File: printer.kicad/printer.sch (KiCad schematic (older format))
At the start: 12 parts

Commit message: Reimplement ZX Spectrum bus interface
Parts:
- removed U? (x4): D3413A, symbol 74xx_IEEE:7413
- removed U? (x5): D3404A, symbol 74xx_IEEE:7404
- added U? (x2): 74AC373, symbol 74xx:74LS373
- added U? (x8): 74HCT02, symbol 74xx:74HCT02
- added U? (x4): 74HCT00, symbol 74xx:74HCT00
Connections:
- net labels added: DEVICE_RD, DEVICE_WR, ENCODER, MOTOR_SLOW, MOTOR_STOP, PAPER, READY, STYLUS, ~ENCODER_LATCH, ~PAPER_LATCH, ~STYLUS
- net labels removed: READ|WRITE, WR
- wire segments 58 -> 83
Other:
- note added: "Decoding"
- note added: "INPUT"
- note added: "Latches"
- note added: "OUTPUT"
- moved on the sheet: J?, U?

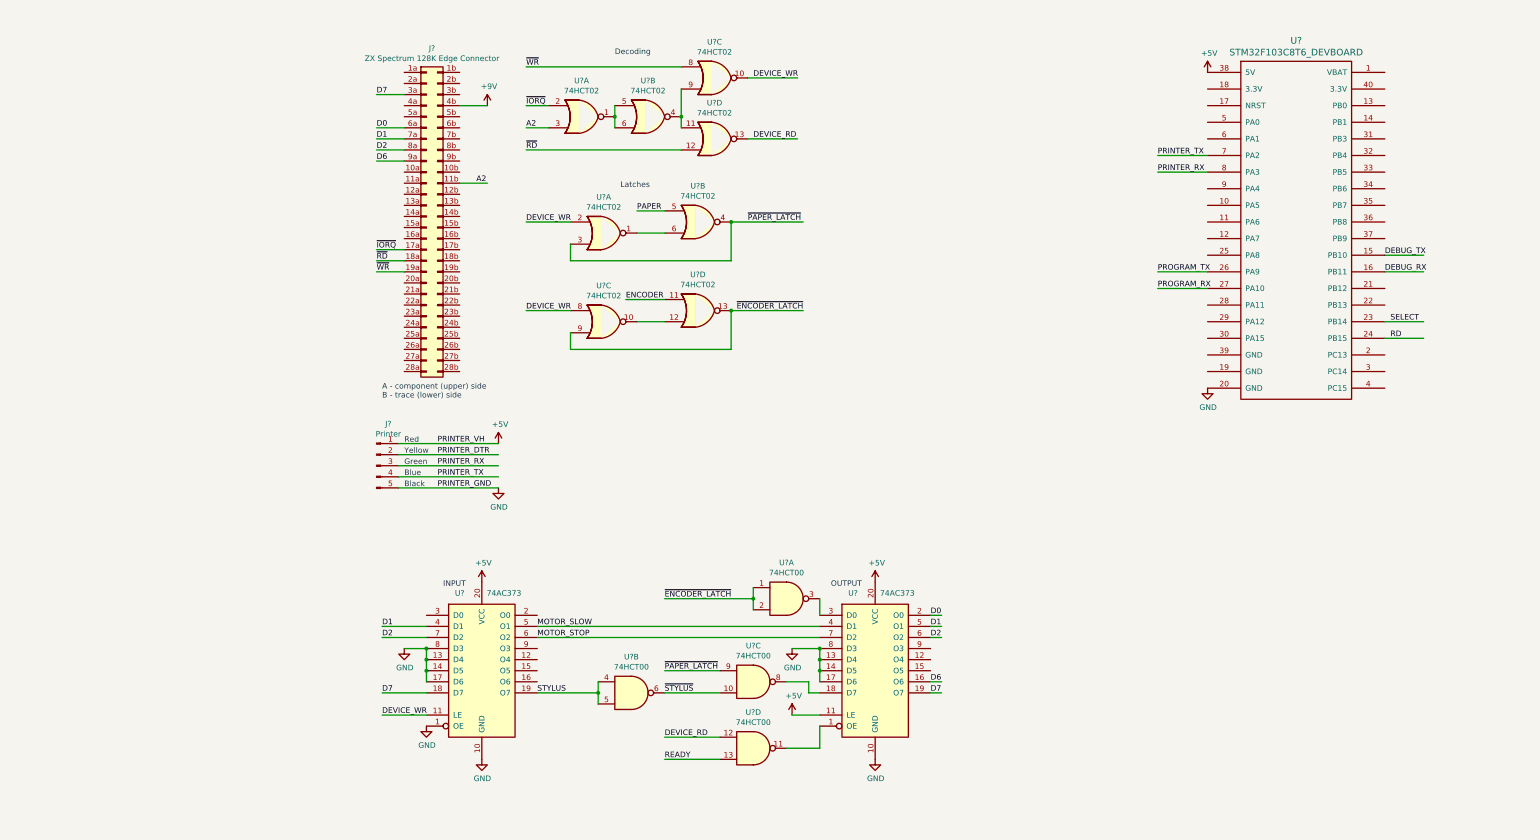
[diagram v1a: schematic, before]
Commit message: Redo latching in HW, understand interface better
Redo latching in hardware, only to understand after testing that the
interface is different. The printer is supposed to reset the latches on
every write regardless of the encoder and paper position.
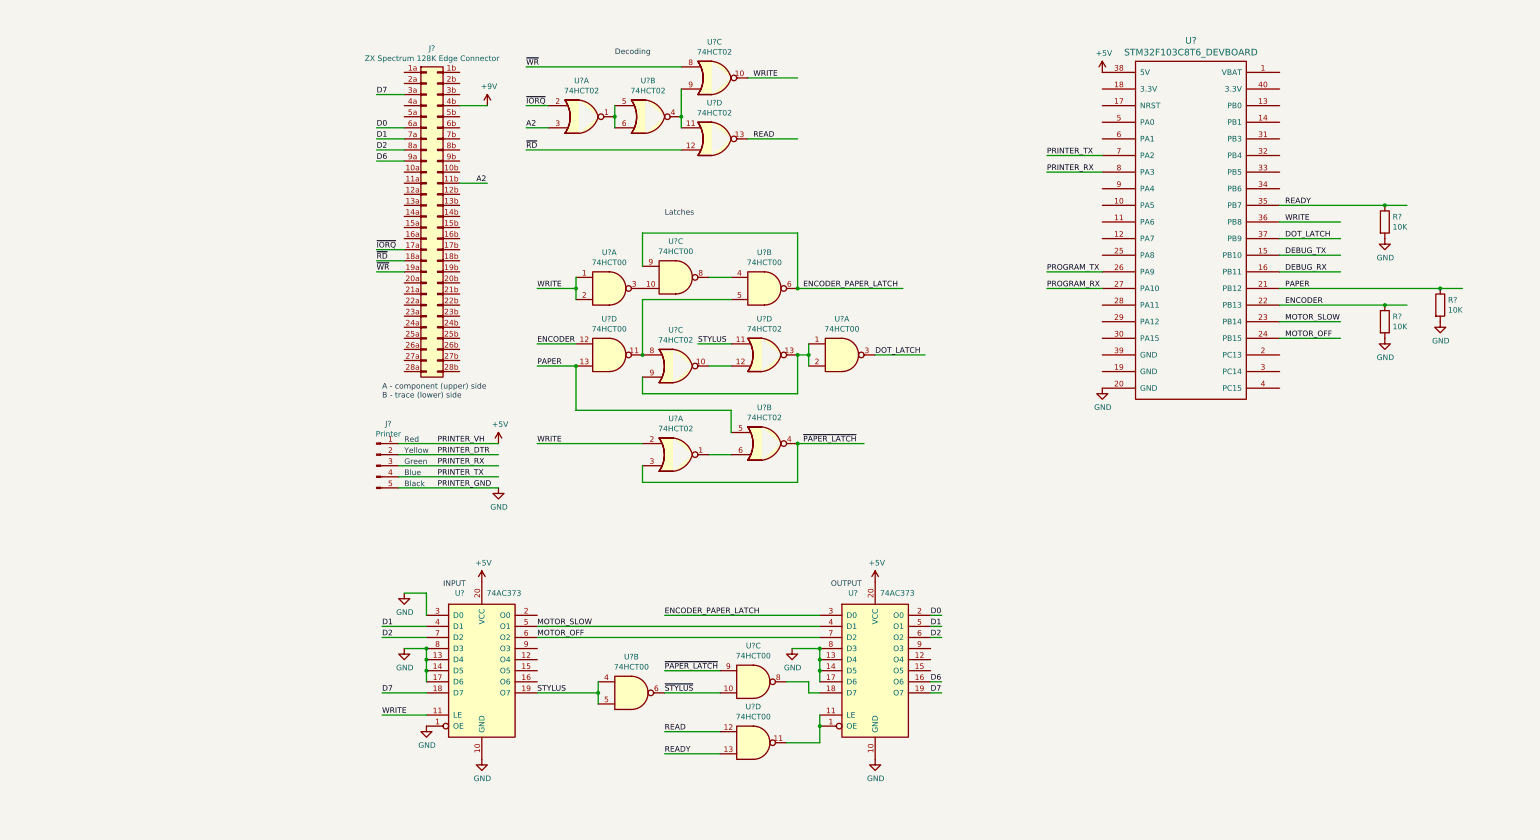
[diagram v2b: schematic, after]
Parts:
- removed U? (x3): 74HCT02, symbol 74xx:74HCT02
- removed U? (x2): 74HCT00, symbol 74xx:74HCT00
- added R? (x3): 10K, symbol Device:R
- added U? (x6): 74HCT00, symbol 74xx:74HCT00
- added U? (x3): 74HCT02, symbol 74xx:74HCT02
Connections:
- net labels added: DOT_LATCH, ENCODER_PAPER_LATCH, MOTOR_OFF, READ, WRITE
- net labels removed: DEVICE_RD, DEVICE_WR, MOTOR_STOP, RD, SELECT, ~ENCODER_LATCH
- wire segments 83 -> 106
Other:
- moved on the sheet: U?, U?A, U?B, U?D

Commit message: Make ZX Printer communication work
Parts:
- removed U? (x5): 74HCT00, symbol 74xx:74HCT00
- removed U? (x4): 74HCT02, symbol 74xx:74HCT02
- added U?: 74HCT00, symbol 74xx:74HCT00
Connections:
- net labels added: ~PAPER
- net labels removed: DOT_LATCH, ENCODER_PAPER_LATCH, ~PAPER_LATCH
- wire segments 106 -> 80
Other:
- note removed: "Latches"
- moved on the sheet: U?, U?B, U?C, U?D

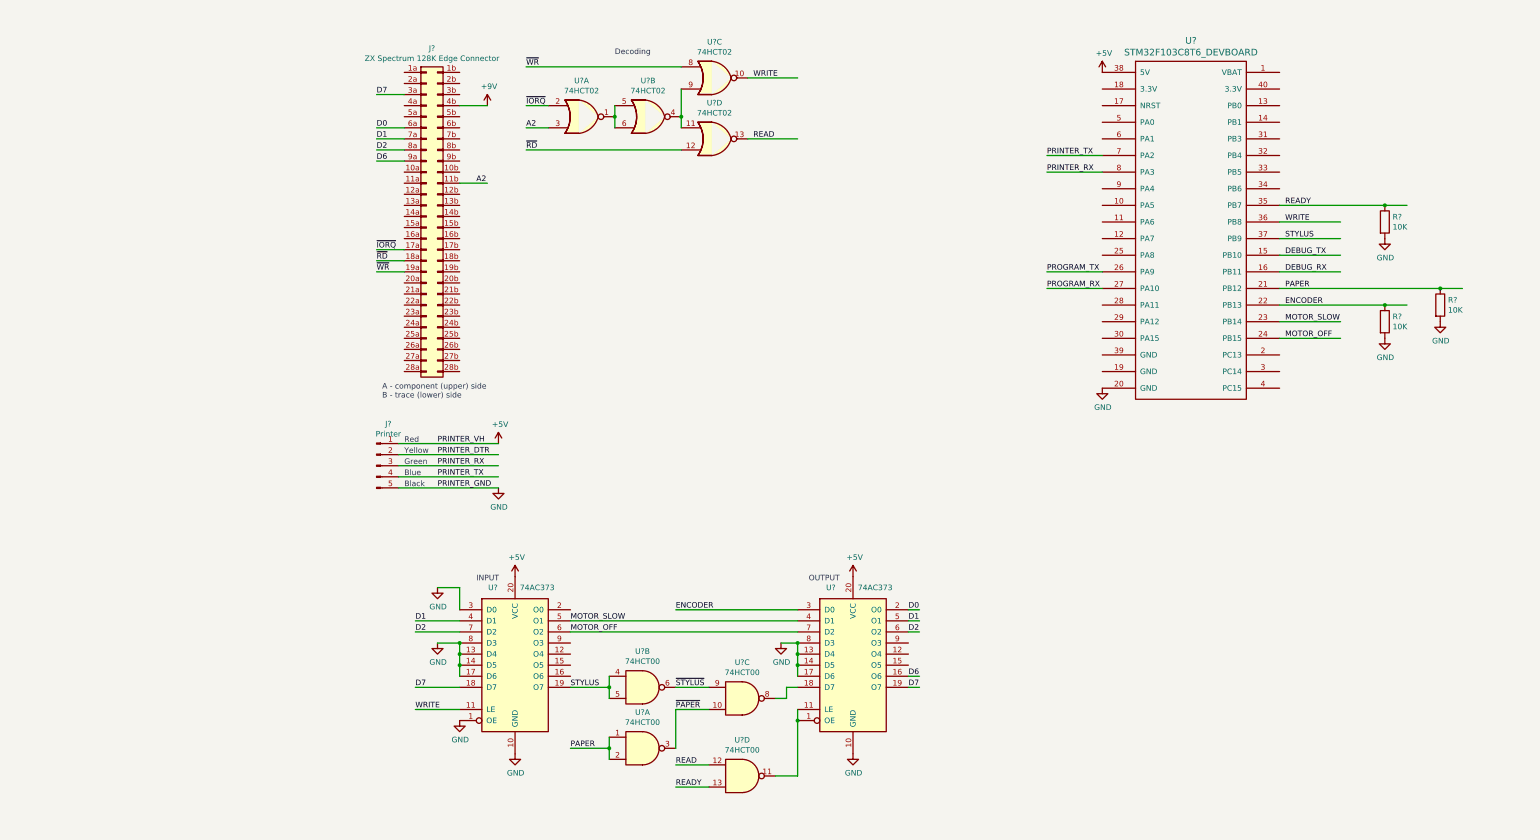
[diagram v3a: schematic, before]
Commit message: Complete schematics for JLCPCB
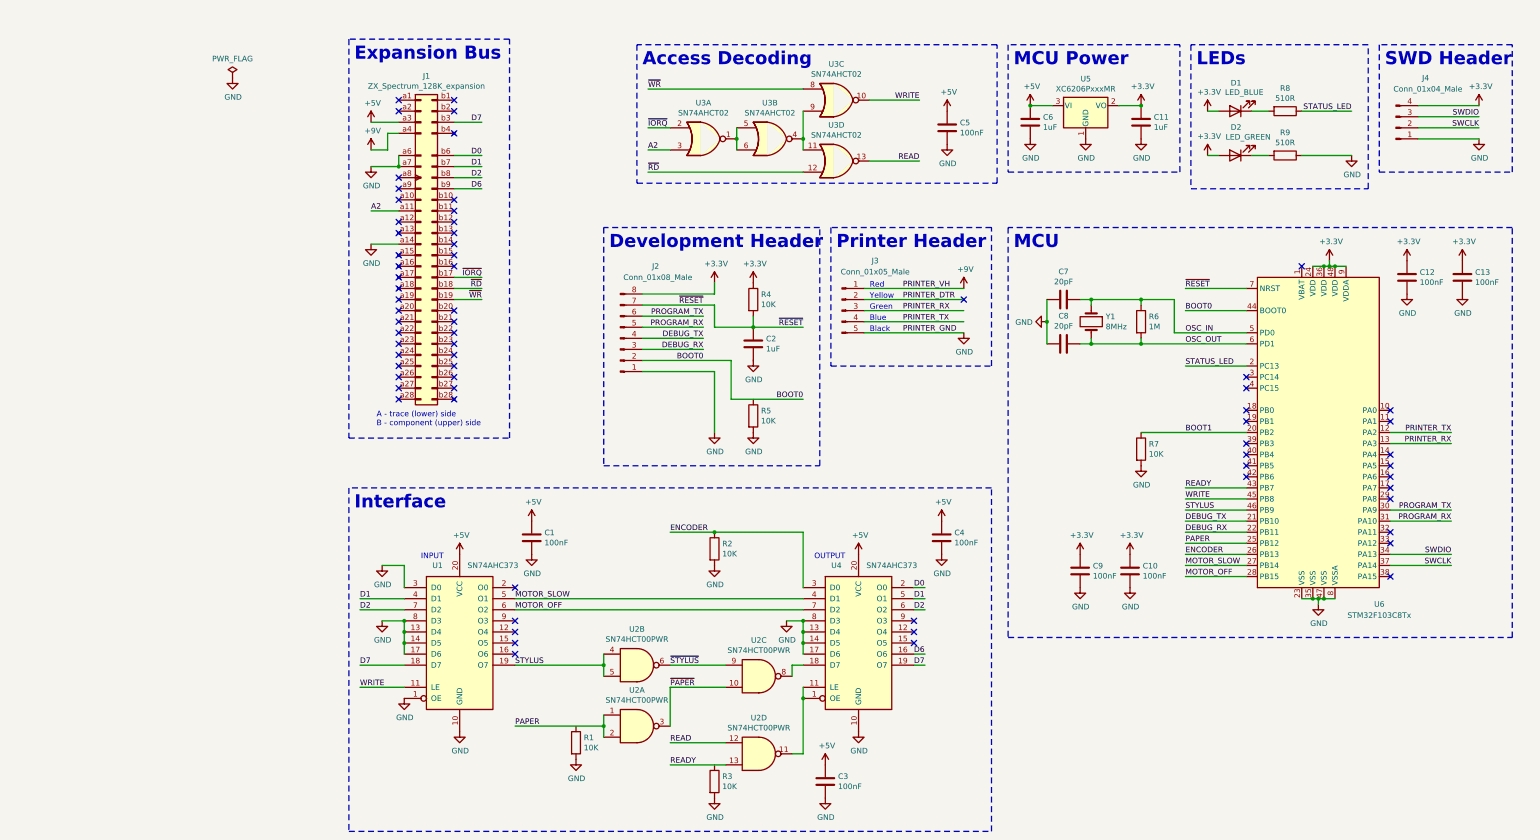
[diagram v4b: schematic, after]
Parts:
- removed J?: ZX Spectrum 128K Edge Connector, symbol Connector_Generic:Conn_02x28_Row_Letter_Last
- removed R? (x2): 10K, symbol Device:R
- removed U?: STM32F103C8T6_DEVBOARD, symbol printer-rescue:STM32F103C8T6_DEVBOARD-printer
- added C1, C10, C12, C13, C3, C4, C5, C9: 100nF, Capacitor_SMD:C_0603_1608Metric, symbol Device:C
- added C11, C2, C6: 1uF, Capacitor_SMD:C_0603_1608Metric, symbol Device:C
- added C7, C8: 20pF, Capacitor_SMD:C_0603_1608Metric, symbol Device:C
- added D1: LED_BLUE, LED_SMD:LED_0603_1608Metric, symbol Device:LED
- added D2: LED_GREEN, LED_SMD:LED_0603_1608Metric, symbol Device:LED
- added J1: ZX_Spectrum_128K_expansion, printer:board_socket, symbol printer:ZX_Spectrum_128K_expansion
- added J2: Conn_01x08_Male, Connector_PinHeader_2.54mm:PinHeader_1x08_P2.54mm_Vertical, symbol Connector:Conn_01x08_Male
- added J4: Conn_01x04_Male, Connector_PinHeader_2.54mm:PinHeader_1x04_P2.54mm_Vertical, symbol Connector:Conn_01x04_Male
- added R1, R3, R4, R5, R7: 10K, Resistor_SMD:R_0603_1608Metric, symbol Device:R
- added R6: 1M, Resistor_SMD:R_0603_1608Metric, symbol Device:R
- added R8, R9: 510R, Resistor_SMD:R_0603_1608Metric, symbol Device:R
- added U5: XC6206PxxxMR, Package_TO_SOT_SMD:SOT-23, symbol Master_Regulator_Linear:XC6206PxxxMR
- added U6: STM32F103C8Tx, Package_QFP:LQFP-48_7x7mm_P0.5mm, symbol MCU_ST_STM32F1:STM32F103C8Tx
- added Y1: 8MHz, Crystal:Crystal_SMD_5032-2Pin_5.0x3.2mm, symbol Device:Crystal
- J3: renamed from J?; value Printer -> Conn_01x05_Male; footprint (none) -> Connector_JST:JST_XH_B5B-XH-A_1x05_P2.50mm_Vertical
- R2: renamed from R?; footprint (none) -> Resistor_SMD:R_0603_1608Metric; LCSC (none) -> C25804
- U1, U4: renamed from U?; value 74AC373 -> SN74AHC373; footprint (none) -> Package_SO:TSSOP-20_4.4x6.5mm_P0.65mm; LCSC (none) -> C80242
- U2: renamed from U?; value 74HCT00 -> SN74HCT00PWR; footprint (none) -> Package_SO:TSSOP-14_4.4x5mm_P0.65mm; LCSC (none) -> C131694
- U3: renamed from U?; value 74HCT02 -> SN74AHCT02; footprint (none) -> Package_SO:TSSOP-14_4.4x5mm_P0.65mm; LCSC (none) -> C87964
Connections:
- net labels added: +3.3V, BOOT0, BOOT1, OSC_IN, OSC_OUT, STATUS_LED, SWCLK, SWDIO, ~IORQ, ~RD, ~RESET, ~WR
- net labels removed: ~IORQ~, ~RD~, ~WR~
- wire segments 80 -> 142
- no-connect marks 0 -> 68
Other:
- note added: "A - trace (lower) side\nB - component (upper) side\n"
- note added: "Access Decoding"
- note added: "Development Header"
- note added: "Expansion Bus"
- note added: "Interface"
- note added: "LEDs"
- note added: "MCU"
- note added: "MCU Power"
- note added: "Printer Header"
- note added: "SWD Header"
- note removed: "A - component (upper) side\nB - trace (lower) side"
- note removed: "Decoding"
- moved on the sheet: J3, R2, U1, U2A, U2B, U2C, U2D, U3A, U3B, U3C, U3D, U4

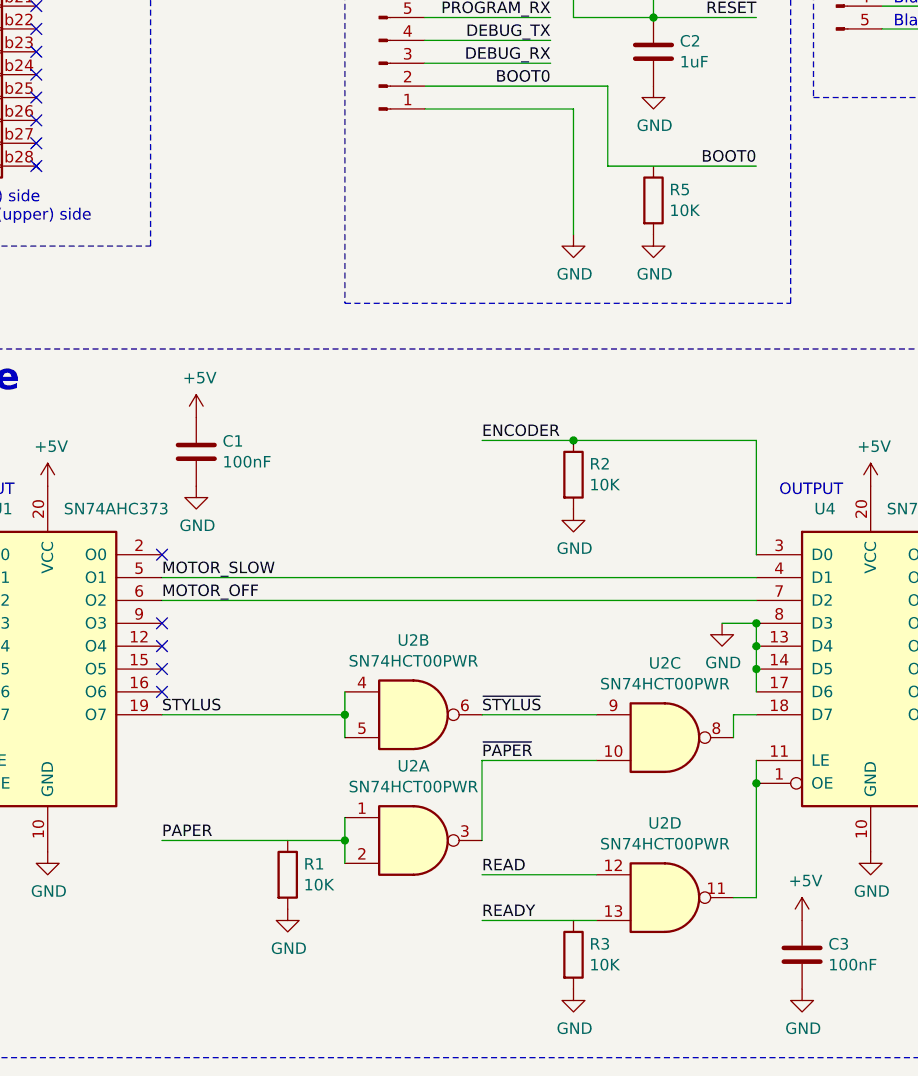
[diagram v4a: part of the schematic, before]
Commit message: Fix unconnected resistors on schematics
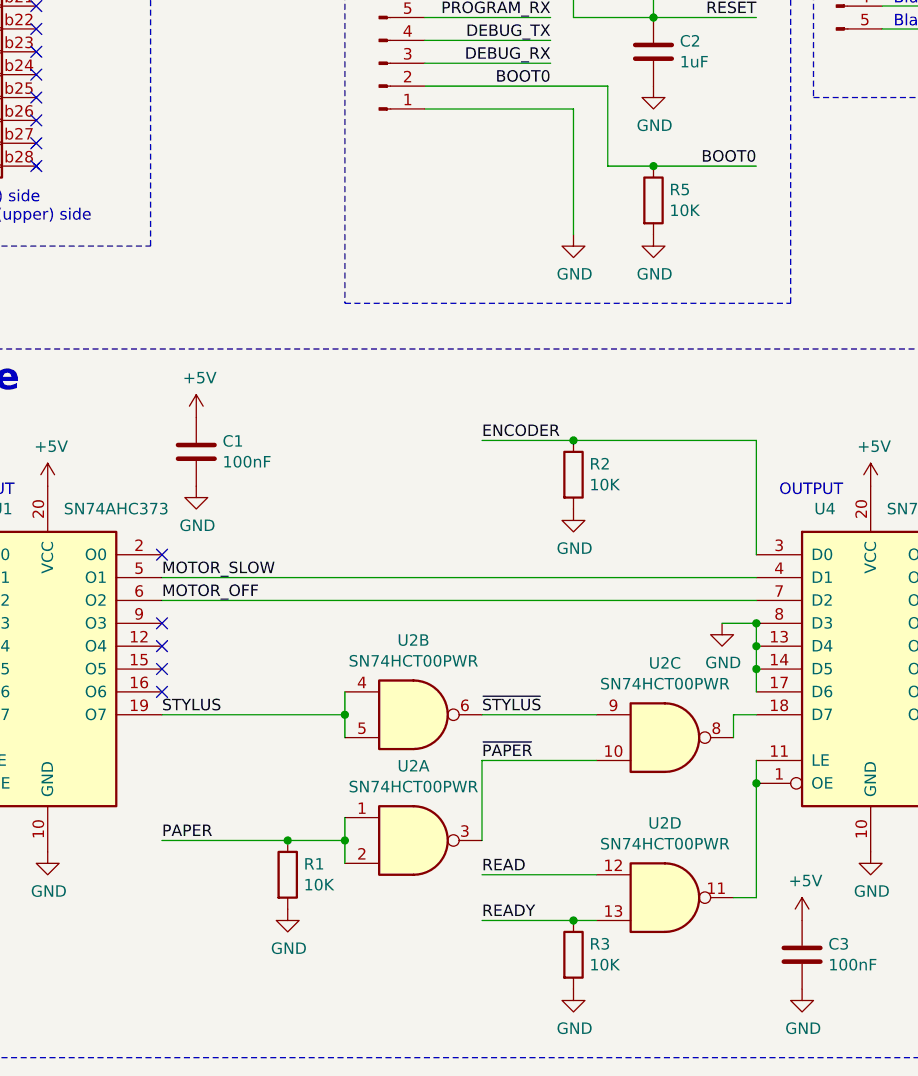
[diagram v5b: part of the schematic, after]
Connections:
- wire segments 142 -> 145
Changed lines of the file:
@@
 NoConn ~ 8700 3600
 Wire Wire Line
-	3500 7100 4000 7100
+	3500 7100 3900 7100
 $Comp
 L Device:R R3
@@
 $EndComp
 Wire Wire Line
-	2100 6750 2900 6750
+	2100 6750 2650 6750
 $Comp
 L Device:R R1
@@
 $EndComp
 Wire Wire Line
-	4050 3800 4700 3800
+	4050 3800 4250 3800
 $Comp
 L Device:R R5
@@
 	-1   0    0    1
 $EndComp
+Connection ~ 3900 7100
+Wire Wire Line
+	3900 7100 4000 7100
+Connection ~ 2650 6750
+Wire Wire Line
+	2650 6750 2900 6750
+Connection ~ 4250 3800
+Wire Wire Line
+	4250 3800 4700 3800
 $EndSCHEMATC

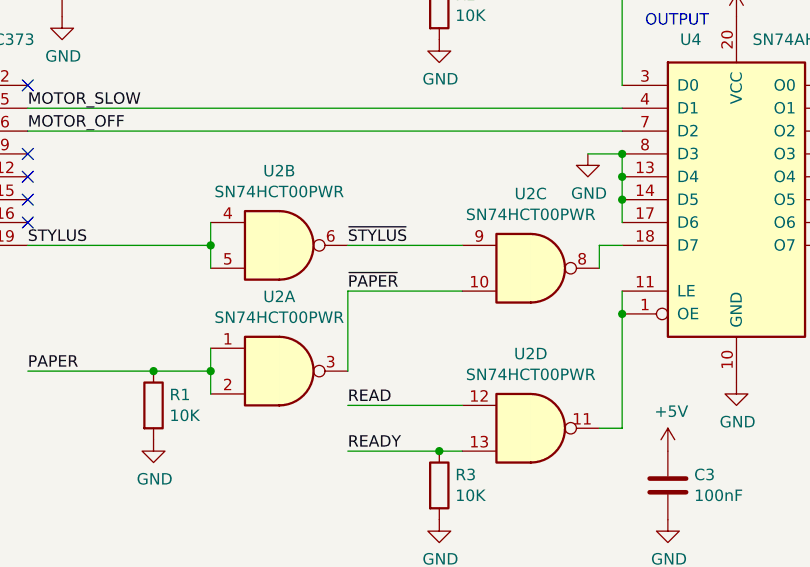
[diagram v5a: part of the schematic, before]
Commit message: Shorten SN74HCT00PWR to SN74HCT00
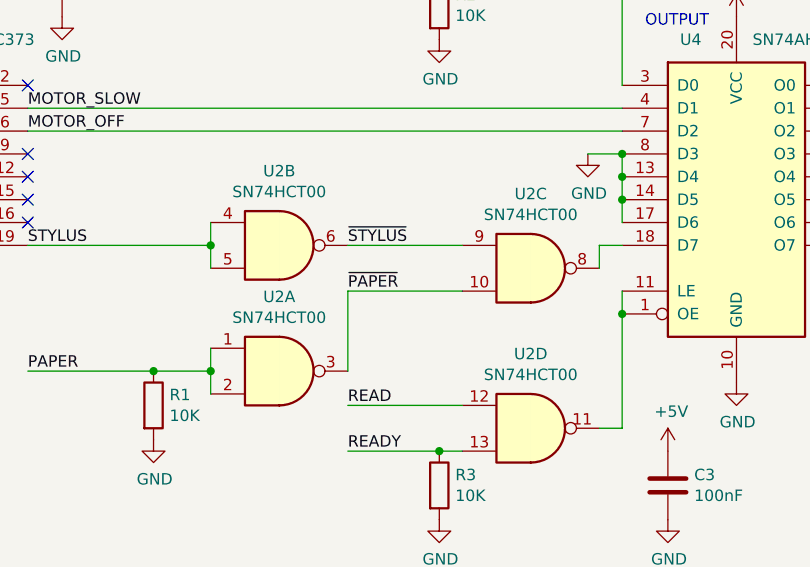
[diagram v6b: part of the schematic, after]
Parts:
- U2: value SN74HCT00PWR -> SN74HCT00
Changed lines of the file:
@@
 P 4300 6300
 F 0 "U2" H 4300 6625 50  0000 C CNN
-F 1 "SN74HCT00PWR" H 4300 6534 50  0000 C CNN
+F 1 "SN74HCT00" H 4300 6534 50  0000 C CNN
 F 2 "Package_SO:TSSOP-14_4.4x5mm_P0.65mm" H 4300 6300 50  0001 C CNN
 F 3 "https://www.ti.com/lit/ds/symlink/sn74hct00.pdf" H 4300 6300 50  0001 C CNN
@@
 P 4300 7000
 F 0 "U2" H 4300 7325 50  0000 C CNN
-F 1 "SN74HCT00PWR" H 4300 7234 50  0000 C CNN
+F 1 "SN74HCT00" H 4300 7234 50  0000 C CNN
 F 2 "Package_SO:TSSOP-14_4.4x5mm_P0.65mm" H 4300 7000 50  0001 C CNN
 F 3 "https://www.ti.com/lit/ds/symlink/sn74hct00.pdf" H 4300 7000 50  0001 C CNN
@@
 P 3200 6200
 F 0 "U2" H 3200 6525 50  0000 C CNN
-F 1 "SN74HCT00PWR" H 3200 6434 50  0000 C CNN
+F 1 "SN74HCT00" H 3200 6434 50  0000 C CNN
 F 2 "Package_SO:TSSOP-14_4.4x5mm_P0.65mm" H 3200 6200 50  0001 C CNN
 F 3 "https://www.ti.com/lit/ds/symlink/sn74hct00.pdf" H 3200 6200 50  0001 C CNN
@@
 P 3200 6750
 F 0 "U2" H 3200 7075 50  0000 C CNN
-F 1 "SN74HCT00PWR" H 3200 6984 50  0000 C CNN
+F 1 "SN74HCT00" H 3200 6984 50  0000 C CNN
 F 2 "Package_SO:TSSOP-14_4.4x5mm_P0.65mm" H 3200 6750 50  0001 C CNN
 F 3 "https://www.ti.com/lit/ds/symlink/sn74hct00.pdf" H 3200 6750 50  0001 C CNN
